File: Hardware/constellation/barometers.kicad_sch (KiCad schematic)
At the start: 8 parts, among them U2 ICM-45686, U3 LSM6DSV32X

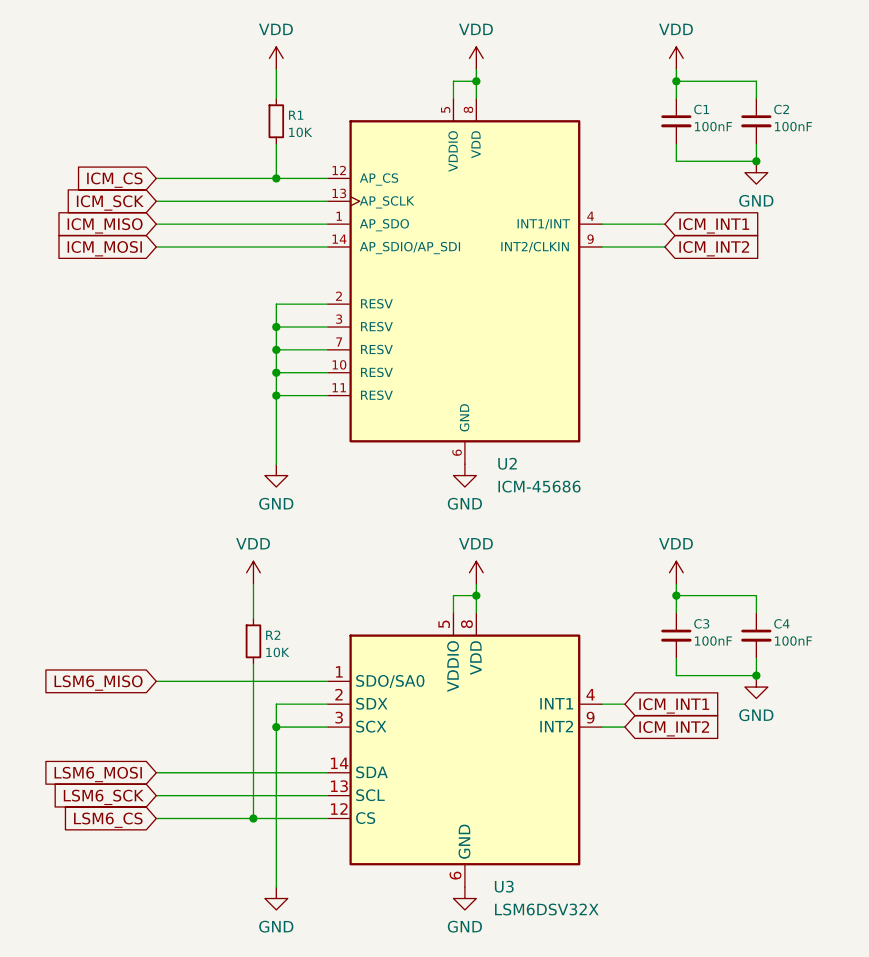
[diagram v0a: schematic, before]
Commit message: finalize baros and add the magnetometer sheet
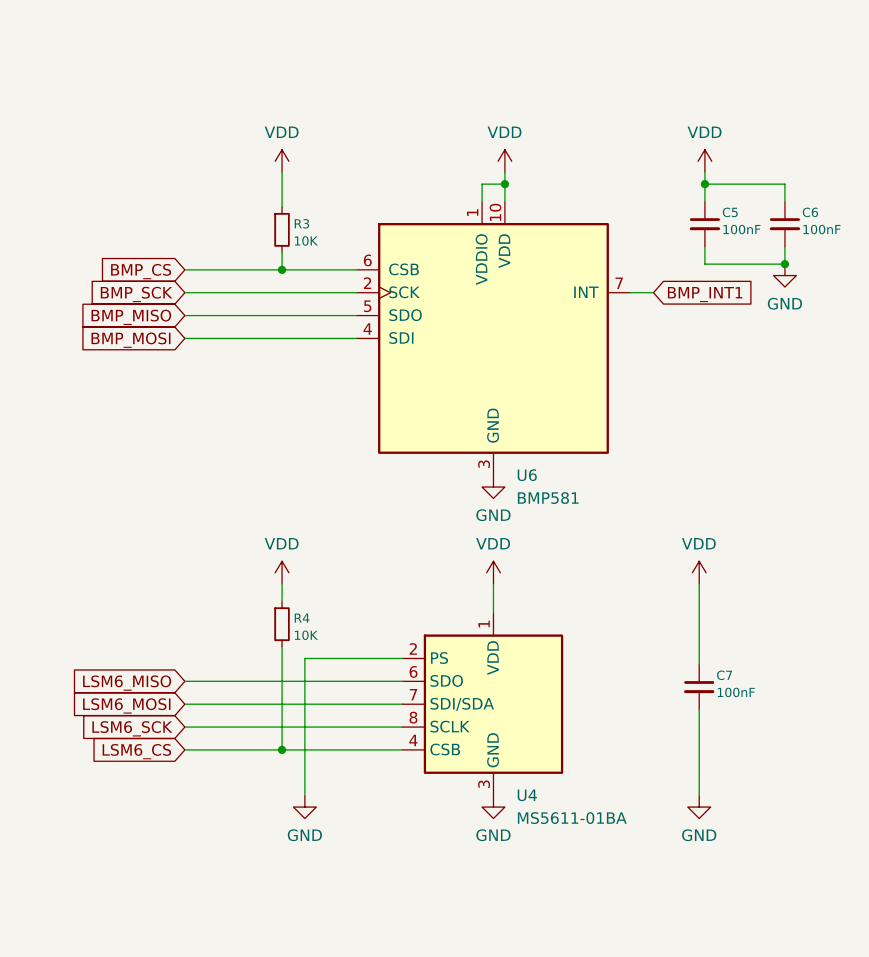
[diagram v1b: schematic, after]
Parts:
- removed C1, C2, C3, C4: 100nF, Capacitor_SMD:C_0402_1005Metric, symbol Device:C_Small
- removed R1, R2: 10K, Resistor_SMD:R_0402_1005Metric_Pad0.72x0.64mm_HandSolder, symbol Device:R_Small
- removed U2: ICM-45686, ICM_45686:IC_ICM-45686, symbol ICM-45686:ICM-45686
- removed U3: LSM6DSV32X, Package_LGA:LGA-14_3x2.5mm_P0.5mm_LayoutBorder3x4y, symbol Sensor_Motion:LSM6DSL
- added C5, C6, C7: 100nF, Capacitor_SMD:C_0402_1005Metric, symbol Device:C_Small
- added R3, R4: 10K, Resistor_SMD:R_0402_1005Metric_Pad0.72x0.64mm_HandSolder, symbol Device:R_Small
- added U4: MS5611-01BA, Package_LGA:LGA-8_3x5mm_P1.25mm, symbol Sensor_Pressure:MS5611-01BA
- added U6: BMP581, BMP581:QFN10_BMP581_BOS-M, symbol BMP581:BMP581
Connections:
- net GND: now also C5.2, C6.2, C7.2, U4.2 (PS), U4.3 (GND), U6.3 (GND), U6.8 (GND), U6.9 (GND)
- net LSM6_CS: now also R4.2, U4.4 (CSB), U4.5 (CSB)
- net LSM6_MISO: now also U4.6 (SDO)
- net LSM6_MOSI: now also U4.7 (SDI/SDA)
- net LSM6_SCK: now also U4.8 (SCLK)
- net VDD: now also C5.1, C6.1, C7.1, R3.1, R4.1, U4.1 (VDD), U6.1 (VDDIO), U6.10 (VDD)
- new net BMP_CS: R3.2, U6.6 (CSB)
- new net BMP_INT1: U6.7 (INT)
- new net BMP_MISO: U6.5 (SDO)
- new net BMP_MOSI: U6.4 (SDI)
- new net BMP_SCK: U6.2 (SCK)
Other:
- title: Inertial Measurement Unit Array -> Barometer Unit Array

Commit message: shift to hierarchial design, add GNSS, mag, accel
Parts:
- removed C5, C6, C7: 100nF, Capacitor_SMD:C_0402_1005Metric, symbol Device:C_Small
- removed R3, R4: 10K, Resistor_SMD:R_0402_1005Metric_Pad0.72x0.64mm_HandSolder, symbol Device:R_Small
- removed U4: MS5611-01BA, Package_LGA:LGA-8_3x5mm_P1.25mm, symbol Sensor_Pressure:MS5611-01BA
- removed U6: BMP581, BMP581:QFN10_BMP581_BOS-M, symbol BMP581:BMP581
- added C12, C13, C14: 100nF, Capacitor_SMD:C_0402_1005Metric, symbol Device:C_Small
- added R10, R9: 10K, Resistor_SMD:R_0402_1005Metric_Pad0.72x0.64mm_HandSolder, symbol Device:R_Small
- added U10: MS5611-01BA, Package_LGA:LGA-8_3x5mm_P1.25mm, symbol Sensor_Pressure:MS5611-01BA
- added U9: BMP581, BMP581:QFN10_BMP581_BOS-M, symbol BMP581:BMP581
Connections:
- net BMP_CS: now also R9.2, U9.6 (CSB)
- net BMP_INT1: now also U9.7 (INT)
- net BMP_MISO: now also U9.5 (SDO)
- net BMP_MOSI: now also U9.4 (SDI)
- net BMP_SCK: now also U9.2 (SCK)
- net GND: now also C12.2, C13.2, C14.2, U10.2 (PS), U10.3 (GND), U9.3 (GND), U9.8 (GND), U9.9 (GND)
- net LSM6_CS: now also R10.2, U10.4 (CSB), U10.5 (CSB)
- net LSM6_MISO: now also U10.6 (SDO)
- net LSM6_MOSI: now also U10.7 (SDI/SDA)
- net LSM6_SCK: now also U10.8 (SCLK)
- net VDD: now also C12.1, C13.1, C14.1, R10.1, R9.1, U10.1 (VDD), U9.1 (VDDIO), U9.10 (VDD)
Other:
- title: Barometer Unit Array -> Barometric Unit Array

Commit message: add the hierarchal pins to the imu block
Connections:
- net LSM6_CS renamed MS56_CS
- net LSM6_MISO renamed MS56_MISO
- net LSM6_MOSI renamed MS56_MOSI
- net LSM6_SCK renamed MS56_SCK
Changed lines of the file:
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@@
 		)
 	)
-	(global_label "LSM6_MOSI"
+	(hierarchical_label "BMP_SCK"
 		(shape input)
-		(at 116.205 129.54 180)
-		(fields_autoplaced yes)
+		(at 116.205 83.82 180)
 		(effects
 			(font
@@
 			(justify right)
 		)
-		(property "Intersheetrefs" "${INTERSHEET_REFS}"
-			(at 97.1937 129.54 0)
-			(hide yes)
-			(show_name no)
-			(do_not_autoplace no)
-			(effects
-				(font
-					(size 1.27 1.27)
-				)
-				(justify right)
-			)
-		)
 	)
-	(global_label "LSM6_CS"
+	(hierarchical_label "MS56_SCK"
 		(shape input)
-		(at 116.205 134.62 180)
-		(fields_autoplaced yes)
+		(at 116.205 132.08 180)
 		(effects
 			(font
@@
 			(justify right)
 		)
-		(property "Intersheetrefs" "${INTERSHEET_REFS}"
-			(at 97.1937 134.62 0)
-			(hide yes)
-			(show_name no)
-			(do_not_autoplace no)
-			(effects
-				(font
-					(size 1.27 1.27)
-				)
-				(justify right)
-			)
-		)
 	)
-	(global_label "BMP_INT1"
+	(hierarchical_label "BMP_INT1"
 		(shape input)
 		(at 168.275 83.82 0)
-		(fields_autoplaced yes)
 		(effects
 			(font
@@
 			(justify left)
 		)
-		(property "Intersheetrefs" "${INTERSHEET_REFS}"
-			(at 187.2863 83.82 0)
-			(hide yes)
-			(show_name no)
-			(do_not_autoplace no)
-			(effects
-				(font
-					(size 1.27 1.27)
-				)
-				(justify left)
-			)
-		)
 	)
-	(global_label "LSM6_MISO"
+	(hierarchical_label "BMP_MOSI"
 		(shape input)
-		(at 116.205 127 180)
-		(fields_autoplaced yes)
+		(at 116.205 88.9 180)
 		(effects
 			(font
@@
 			(justify right)
 		)
-		(property "Intersheetrefs" "${INTERSHEET_REFS}"
-			(at 97.1937 127 0)
-			(hide yes)
-			(show_name no)
-			(do_not_autoplace no)
-			(effects
-				(font
-					(size 1.27 1.27)
-				)
-				(justify right)
-			)
-		)
 	)
-	(global_label "BMP_MOSI"
+	(hierarchical_label "MS56_MOSI"
 		(shape input)
-		(at 116.205 88.9 180)
-		(fields_autoplaced yes)
+		(at 116.205 129.54 180)
 		(effects
 			(font
@@
 			(justify right)
 		)
-		(property "Intersheetrefs" "${INTERSHEET_REFS}"
-			(at 97.1937 88.9 0)
-			(hide yes)
-			(show_name no)
-			(do_not_autoplace no)
-			(effects
-				(font
-					(size 1.27 1.27)
-				)
-				(justify right)
-			)
-		)
 	)
-	(global_label "BMP_MISO"
+	(hierarchical_label "BMP_MISO"
 		(shape input)
 		(at 116.205 86.36 180)
-		(fields_autoplaced yes)
 		(effects
 			(font
@@
 			(justify right)
 		)
-		(property "Intersheetrefs" "${INTERSHEET_REFS}"
-			(at 97.1937 86.36 0)
-			(hide yes)
-			(show_name no)
-			(do_not_autoplace no)
-			(effects
-				(font
-					(size 1.27 1.27)
-				)
-				(justify right)
-			)
-		)
 	)
-	(global_label "BMP_SCK"
+	(hierarchical_label "BMP_CS"
 		(shape input)
-		(at 116.205 83.82 180)
-		(fields_autoplaced yes)
+		(at 116.205 81.28 180)
 		(effects
 			(font
@@
 			(justify right)
 		)
-		(property "Intersheetrefs" "${INTERSHEET_REFS}"
-			(at 97.1937 83.82 0)
-			(hide yes)
-			(show_name no)
-			(do_not_autoplace no)
-			(effects
-				(font
-					(size 1.27 1.27)
-				)
-				(justify right)
-			)
-		)
 	)
-	(global_label "LSM6_SCK"
+	(hierarchical_label "MS56_CS"
 		(shape input)
-		(at 116.205 132.08 180)
-		(fields_autoplaced yes)
+		(at 116.205 134.62 180)
 		(effects
 			(font
@@
 			(justify right)
 		)
-		(property "Intersheetrefs" "${INTERSHEET_REFS}"
-			(at 97.1937 132.08 0)
-			(hide yes)
-			(show_name no)
-			(do_not_autoplace no)
-			(effects
-				(font
-					(size 1.27 1.27)
-				)
-				(justify right)
-			)
-		)
 	)
-	(global_label "BMP_CS"
+	(hierarchical_label "MS56_MISO"
 		(shape input)
-		(at 116.205 81.28 180)
-		(fields_autoplaced yes)
+		(at 116.205 127 180)
 		(effects
 			(font
@@
 			(justify right)
 		)
-		(property "Intersheetrefs" "${INTERSHEET_REFS}"
-			(at 97.1937 81.28 0)
-			(hide yes)
-			(show_name no)
-			(do_not_autoplace no)
-			(effects
-				(font
-					(size 1.27 1.27)
-				)
-				(justify right)
-			)
-		)
 	)

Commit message: add gnss short detection and lna_en supervisor
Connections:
- net BMP_INT1 renamed BMP_INT
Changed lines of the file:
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@@
 		)
 	)
-	(hierarchical_label "BMP_INT1"
+	(hierarchical_label "BMP_INT"
 		(shape input)
 		(at 168.275 83.82 0)

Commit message: add lr2021 footprint and comms
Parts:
- renumbered C12 to C5, C13 to C6, C14 to C7, R9 to R3, R10 to R4, U9 to U4, U10 to U5
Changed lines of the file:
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@@
 		(in_pos_files yes)
 		(dnp no)
-		(property "Reference" "C12"
+		(property "Reference" "C5"
 			(at 175.26 126.365 0)
 			(show_name no)
@@
 			(project "constellation"
 				(path "/ba226b81-7f6b-4f1e-964f-d5311904768c/e58ad819-5158-48e0-9ab4-5c84433e006e"
-					(reference "C12")
+					(reference "C5")
 					(unit 1)
 				)
@@
 		(dnp no)
 		(fields_autoplaced yes)
-		(property "Reference" "#PWR052"
+		(property "Reference" "#PWR013"
 			(at 127 74.295 0)
 			(hide yes)
@@
 			(project "constellation"
 				(path "/ba226b81-7f6b-4f1e-964f-d5311904768c/e58ad819-5158-48e0-9ab4-5c84433e006e"
-					(reference "#PWR052")
+					(reference "#PWR013")
 					(unit 1)
 				)
@@
 		(dnp no)
 		(fields_autoplaced yes)
-		(property "Reference" "#PWR057"
+		(property "Reference" "#PWR018"
 			(at 150.495 146.05 0)
 			(hide yes)
@@
 			(project "constellation"
 				(path "/ba226b81-7f6b-4f1e-964f-d5311904768c/e58ad819-5158-48e0-9ab4-5c84433e006e"
-					(reference "#PWR057")
+					(reference "#PWR018")
 					(unit 1)
 				)
@@
 		(dnp no)
 		(fields_autoplaced yes)
-		(property "Reference" "#PWR061"
+		(property "Reference" "#PWR022"
 			(at 173.99 74.295 0)
 			(hide yes)
@@
 			(project "constellation"
 				(path "/ba226b81-7f6b-4f1e-964f-d5311904768c/e58ad819-5158-48e0-9ab4-5c84433e006e"
-					(reference "#PWR061")
+					(reference "#PWR022")
 					(unit 1)
 				)
@@
 		(dnp no)
 		(fields_autoplaced yes)
-		(property "Reference" "#PWR062"
+		(property "Reference" "#PWR023"
 			(at 182.88 86.995 0)
 			(hide yes)
@@
 			(project "constellation"
 				(path "/ba226b81-7f6b-4f1e-964f-d5311904768c/e58ad819-5158-48e0-9ab4-5c84433e006e"
-					(reference "#PWR062")
+					(reference "#PWR023")
 					(unit 1)
 				)
@@
 		(in_pos_files yes)
 		(dnp no)
-		(property "Reference" "U10"
+		(property "Reference" "U5"
 			(at 153.035 139.7 0)
 			(show_name no)
@@
 			(project "constellation"
 				(path "/ba226b81-7f6b-4f1e-964f-d5311904768c/e58ad819-5158-48e0-9ab4-5c84433e006e"
-					(reference "U10")
+					(reference "U5")
 					(unit 1)
 				)
@@
 		(dnp no)
 		(fields_autoplaced yes)
-		(property "Reference" "#PWR060"
+		(property "Reference" "#PWR021"
 			(at 173.355 146.05 0)
 			(hide yes)
@@
 			(project "constellation"
 				(path "/ba226b81-7f6b-4f1e-964f-d5311904768c/e58ad819-5158-48e0-9ab4-5c84433e006e"
-					(reference "#PWR060")
+					(reference "#PWR021")
 					(unit 1)
 				)
@@
 		(in_pos_files yes)
 		(dnp no)
-		(property "Reference" "#PWR056"
+		(property "Reference" "#PWR017"
 			(at 150.495 120.015 0)
 			(hide yes)
@@
 			(project "constellation"
 				(path "/ba226b81-7f6b-4f1e-964f-d5311904768c/e58ad819-5158-48e0-9ab4-5c84433e006e"
-					(reference "#PWR056")
+					(reference "#PWR017")
 					(unit 1)
 				)
@@
 		(in_pos_files yes)
 		(dnp no)
-		(property "Reference" "R10"
+		(property "Reference" "R4"
 			(at 128.27 120.0151 0)
 			(show_name no)
@@
 			(project "constellation"
 				(path "/ba226b81-7f6b-4f1e-964f-d5311904768c/e58ad819-5158-48e0-9ab4-5c84433e006e"
-					(reference "R10")
+					(reference "R4")
 					(unit 1)
 				)
@@
 		(dnp no)
 		(fields_autoplaced yes)
-		(property "Reference" "U9"
+		(property "Reference" "U4"
 			(at 153.035 104.14 0)
 			(show_name no)
@@
 			(project "constellation"
 				(path "/ba226b81-7f6b-4f1e-964f-d5311904768c/e58ad819-5158-48e0-9ab4-5c84433e006e"
-					(reference "U9")
+					(reference "U4")
 					(unit 1)
 				)
@@
 		(in_pos_files yes)
 		(dnp no)
-		(property "Reference" "#PWR058"
+		(property "Reference" "#PWR019"
 			(at 151.765 74.295 0)
 			(hide yes)
@@
 			(project "constellation"
 				(path "/ba226b81-7f6b-4f1e-964f-d5311904768c/e58ad819-5158-48e0-9ab4-5c84433e006e"
-					(reference "#PWR058")
+					(reference "#PWR019")
 					(unit 1)
 				)
@@
 		(in_pos_files yes)
 		(dnp no)
-		(property "Reference" "R9"
+		(property "Reference" "R3"
 			(at 128.27 76.2001 0)
 			(show_name no)
@@
 			(project "constellation"
 				(path "/ba226b81-7f6b-4f1e-964f-d5311904768c/e58ad819-5158-48e0-9ab4-5c84433e006e"
-					(reference "R9")
+					(reference "R3")
 					(unit 1)
 				)
@@
 		(dnp no)
 		(fields_autoplaced yes)
-		(property "Reference" "#PWR054"
+		(property "Reference" "#PWR015"
 			(at 129.54 146.05 0)
 			(hide yes)
@@
 			(project "constellation"
 				(path "/ba226b81-7f6b-4f1e-964f-d5311904768c/e58ad819-5158-48e0-9ab4-5c84433e006e"
-					(reference "#PWR054")
+					(reference "#PWR015")
 					(unit 1)
 				)
@@
 		(in_pos_files yes)
 		(dnp no)
-		(property "Reference" "C13"
+		(property "Reference" "C6"
 			(at 175.895 74.93 0)
 			(show_name no)
@@
 			(project "constellation"
 				(path "/ba226b81-7f6b-4f1e-964f-d5311904768c/e58ad819-5158-48e0-9ab4-5c84433e006e"
-					(reference "C13")
+					(reference "C6")
 					(unit 1)
 				)
@@
 		(dnp no)
 		(fields_autoplaced yes)
-		(property "Reference" "#PWR053"
+		(property "Reference" "#PWR014"
 			(at 127 120.015 0)
 			(hide yes)
@@
 			(project "constellation"
 				(path "/ba226b81-7f6b-4f1e-964f-d5311904768c/e58ad819-5158-48e0-9ab4-5c84433e006e"
-					(reference "#PWR053")
+					(reference "#PWR014")
 					(unit 1)
 				)
@@
 		(dnp no)
 		(fields_autoplaced yes)
-		(property "Reference" "#PWR059"
+		(property "Reference" "#PWR020"
 			(at 173.355 120.015 0)
 			(hide yes)
@@
 			(project "constellation"
 				(path "/ba226b81-7f6b-4f1e-964f-d5311904768c/e58ad819-5158-48e0-9ab4-5c84433e006e"
-					(reference "#PWR059")
+					(reference "#PWR020")
 					(unit 1)
 				)
@@
 		(dnp no)
 		(fields_autoplaced yes)
-		(property "Reference" "#PWR055"
+		(property "Reference" "#PWR016"
 			(at 150.495 110.49 0)
 			(hide yes)
@@
 			(project "constellation"
 				(path "/ba226b81-7f6b-4f1e-964f-d5311904768c/e58ad819-5158-48e0-9ab4-5c84433e006e"
-					(reference "#PWR055")
+					(reference "#PWR016")
 					(unit 1)
 				)
@@
 		(in_pos_files yes)
 		(dnp no)
-		(property "Reference" "C14"
+		(property "Reference" "C7"
 			(at 184.785 74.93 0)
 			(show_name no)
@@
 			(project "constellation"
 				(path "/ba226b81-7f6b-4f1e-964f-d5311904768c/e58ad819-5158-48e0-9ab4-5c84433e006e"
-					(reference "C14")
-					(unit 1)
-				)
+					(reference "C7")
+					(unit 1)
+				)

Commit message: add pyro stuff, start system power
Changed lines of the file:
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@@
 	)
 	(hierarchical_label "BMP_INT"
-		(shape input)
+		(shape output)
 		(at 168.275 83.82 0)
 		(effects
@@
 	)
 	(hierarchical_label "BMP_MISO"
-		(shape input)
+		(shape output)
 		(at 116.205 86.36 180)
 		(effects
@@
 	)
 	(hierarchical_label "MS56_MISO"
-		(shape input)
+		(shape output)
 		(at 116.205 127 180)
 		(effects
